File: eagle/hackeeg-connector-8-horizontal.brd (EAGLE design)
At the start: 114.6 x 27.9 mm, 21 parts

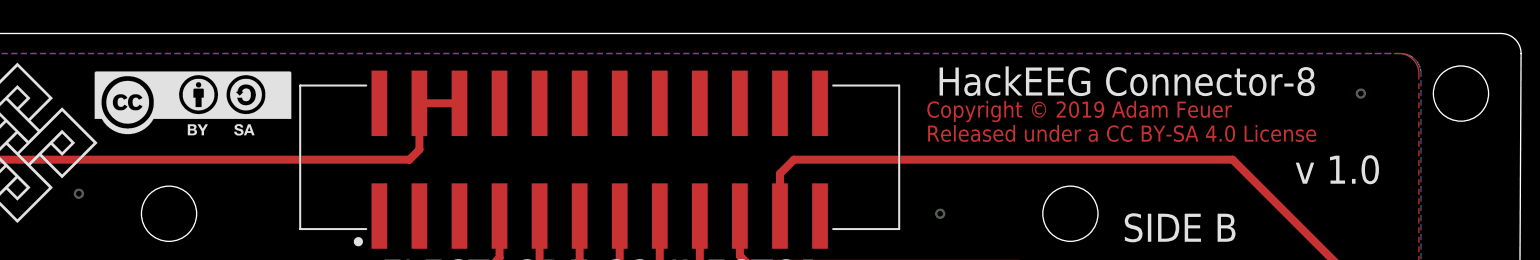
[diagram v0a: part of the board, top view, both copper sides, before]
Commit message: relicense to CERN OHL 1.2 - sch and brd
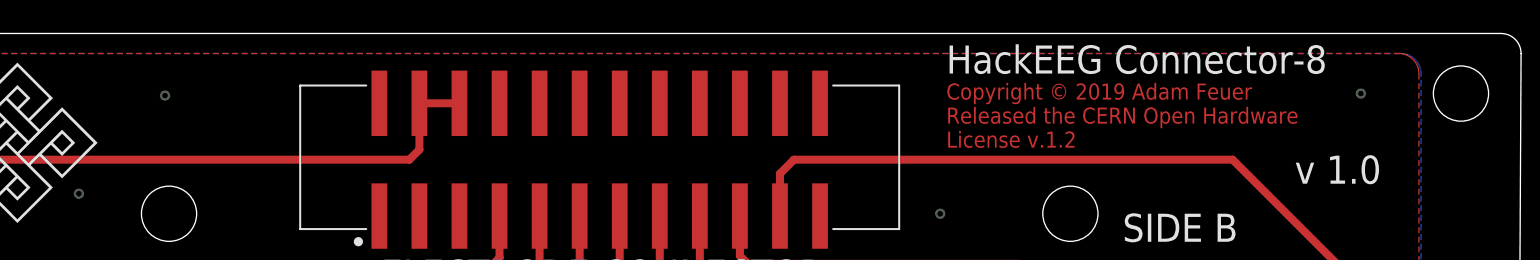
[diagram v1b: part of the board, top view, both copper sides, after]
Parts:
- removed FRAME1: FRAME-LETTER, SparkFun-Aesthetics:CREATIVE_COMMONS
- removed U$13: CC-BY-SA, creative-commons:CC-BY-SA
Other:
- board text added: "Copyright © 2019 Adam Feuer Released the CERN Open Hardware License v.1.2"
- board text removed: "Copyright © 2019 Adam Feuer Released under a CC BY-SA 4.0 License"
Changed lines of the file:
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@@
 <board>
 <plain>
-<text x="76.581" y="23.622" size="1.016" layer="1">Copyright © 2019 Adam Feuer
-Released under a CC BY-SA 4.0 License</text>
+<text x="77.851" y="23.241" size="1.016" layer="1" font="vector" ratio="13">Copyright © 2019 Adam Feuer
+Released the CERN Open Hardware
+License v.1.2</text>
 <hole x="3.81" y="26.67" drill="3.49999375"/>
 <hole x="3.81" y="6.35" drill="3.49999375"/>
@@
 <dimension x1="-2.54" y1="30.48" x2="-2.54" y2="2.54" x3="-8.89" y3="16.51" textsize="1.778" layer="47" unit="inch"/>
 <text x="99.949" y="20.955" size="1.778" layer="25">v 1.0</text>
-<text x="77.216" y="26.543" size="1.778" layer="25">HackEEG Connector-8</text>
+<text x="77.851" y="27.94" size="1.778" layer="25">HackEEG Connector-8</text>
 </plain>
 <attributes>
@@
 <attribute name="VALUE" x="36.7749" y="14.83696875" size="1.78313125" layer="27"/>
 </element>
-<element name="FRAME1" library="SparkFun-Aesthetics" library_urn="urn:adsk.eagle:library:507" package="CREATIVE_COMMONS" package3d_urn="urn:adsk.eagle:package:37121/1" value="FRAME-LETTER" x="21.59" y="-10.16" smashed="yes"/>
 <element name="IN1P" library="po-37729" package="HEX-110" value="PO37729HEX-110" x="22.86" y="10.16" smashed="yes" rot="MR0">
 <attribute name="NAME" x="26.07" y="14.83" size="1.27" layer="26" rot="MR0"/>
@@
 </element>
 <element name="U$1" library="endless-knot" package="ENDLESSKNOT-MEDIUM" value="ENDLESSKNOTENDLESSKNOT-MEDIUM" x="17.653" y="23.495" smashed="yes"/>
-<element name="U$13" library="creative-commons" package="CC-BY-SA" value="CC-BY-SA" x="23.749" y="23.749" smashed="yes"/>
 <element name="IN8P" library="po-37729" package="HEX-110" value="PO37729HEX-110" x="102.87" y="10.16" smashed="yes" rot="MR0">
 <attribute name="NAME" x="106.08" y="14.83" size="1.27" layer="26" rot="MR0"/>
